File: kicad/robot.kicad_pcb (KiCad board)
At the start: 2 copper layers, 0.4 x 3 mm, 48 parts, among them J2 Adafruit Coil Jumper, J3 Adafruit Coil Jumper, M5 Motor_DC, M6 Motor_DC, M7 Motor_DC, M8 Motor_DC, Q2 NMOS, U10 GY-521, U12 NCP176AMX330TCG, U13 DRV8833PW, U6 DRV8833PW, U8 ESP32-DEVKITC, U9 MCP73831-2-OT

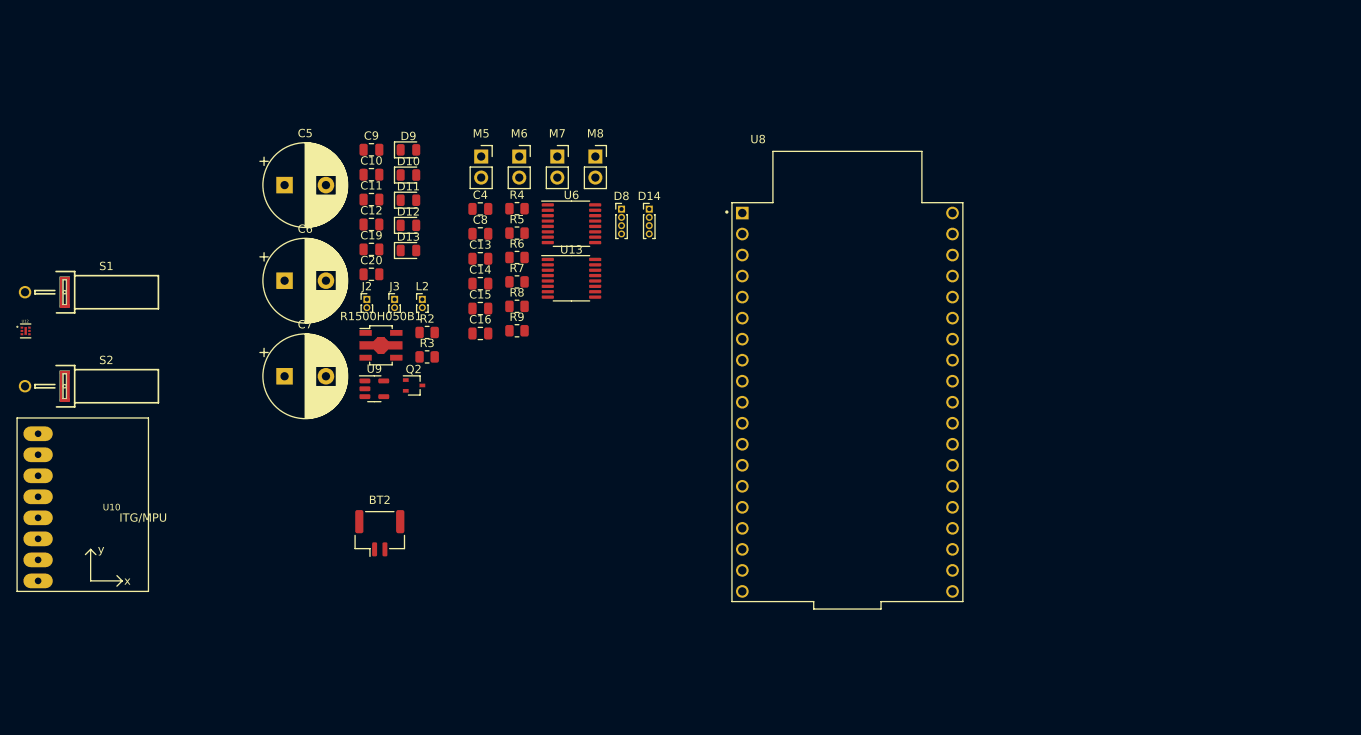
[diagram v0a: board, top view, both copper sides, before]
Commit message: Add board layout
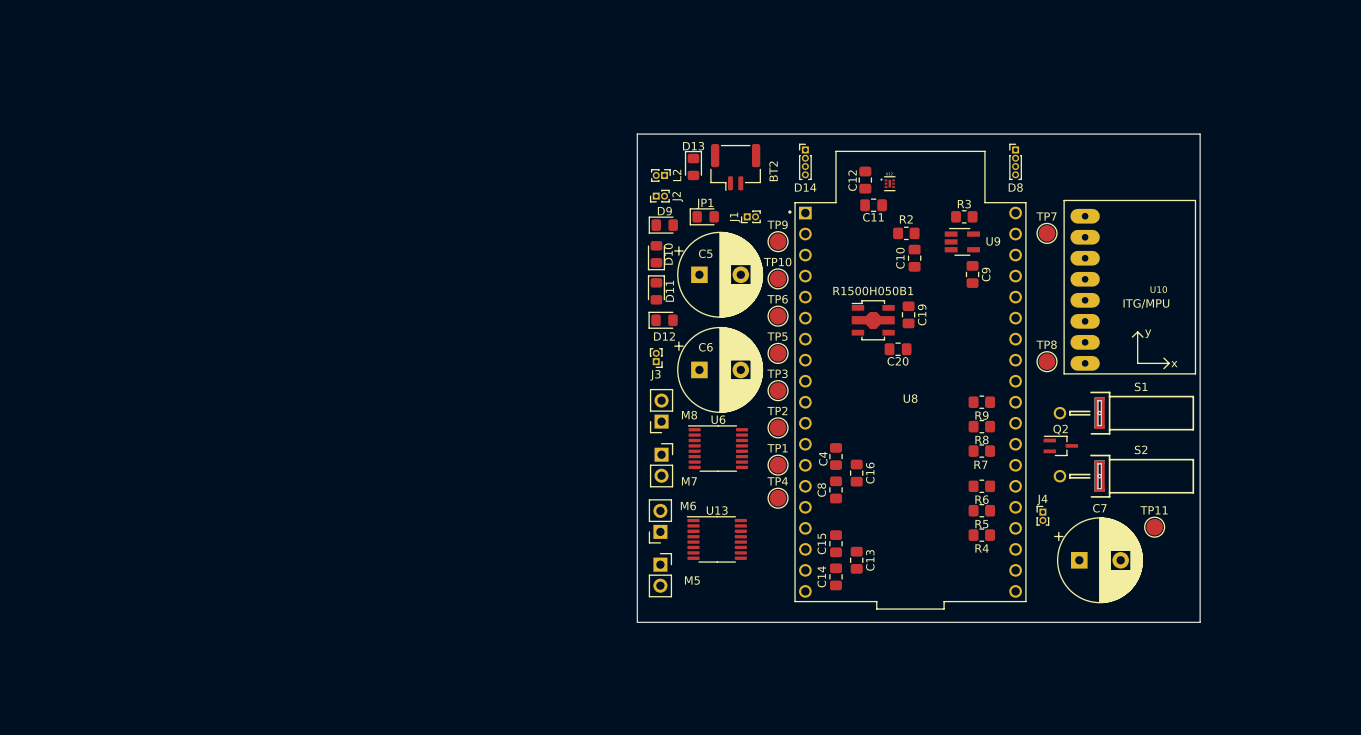
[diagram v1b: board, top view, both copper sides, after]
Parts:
- added J1: Adafruit Coil Jumper, Connector_PinHeader_1.00mm:PinHeader_1x02_P1.00mm_Vertical, F.Cu at (170.8, 66.5)
- added J4: Adafruit Coil Jumper, Connector_PinHeader_1.00mm:PinHeader_1x02_P1.00mm_Vertical, F.Cu at (206.5, 102.2)
- added JP1: SolderJumper_2_Open, Diode_SMD:D_0805_2012Metric_Pad1.15x1.40mm_HandSolder, F.Cu at (165.8, 66.5)
- added TP1: TestPoint, TestPoint:TestPoint_Pad_D2.0mm, F.Cu at (174.5, 96.5)
- added TP10: TestPoint, TestPoint:TestPoint_Pad_D2.0mm, F.Cu at (174.5, 74.0)
- added TP11: TestPoint, TestPoint:TestPoint_Pad_D2.0mm, F.Cu at (220.0, 104.0)
- added TP2: TestPoint, TestPoint:TestPoint_Pad_D2.0mm, F.Cu at (174.5, 92.0)
- added TP3: TestPoint, TestPoint:TestPoint_Pad_D2.0mm, F.Cu at (174.5, 87.5)
- added TP4: TestPoint, TestPoint:TestPoint_Pad_D2.0mm, F.Cu at (174.5, 100.5)
- added TP5: TestPoint, TestPoint:TestPoint_Pad_D2.0mm, F.Cu at (174.5, 83.0)
- added TP6: TestPoint, TestPoint:TestPoint_Pad_D2.0mm, F.Cu at (174.5, 78.5)
- added TP7: TestPoint, TestPoint:TestPoint_Pad_D2.0mm, F.Cu at (207.0, 68.5)
- added TP8: TestPoint, TestPoint:TestPoint_Pad_D2.0mm, F.Cu at (207.0, 84.0)
- added TP9: TestPoint, TestPoint:TestPoint_Pad_D2.0mm, F.Cu at (174.5, 69.5)
- C10, C11, C12, C13, C14, C15, C16, C19, C20, C4, C8, C9: footprint Capacitor_SMD:C_0805_2012Metric -> Capacitor_SMD:C_0805_2012Metric_Pad1.18x1.45mm_HandSolder
- D10, D11, D12, D9: footprint Diode_SMD:D_0805_2012Metric -> Diode_SMD:D_0805_2012Metric_Pad1.15x1.40mm_HandSolder
- D13: footprint LED_SMD:LED_0805_2012Metric -> LED_SMD:LED_0805_2012Metric_Pad1.15x1.40mm_HandSolder
- Q2: footprint Package_TO_SOT_SMD:SOT-323_SC-70 -> Package_TO_SOT_SMD:SOT-323_SC-70_Handsoldering
- R2, R3, R4, R5, R6, R7, R8, R9: footprint Resistor_SMD:R_0805_2012Metric -> Resistor_SMD:R_0805_2012Metric_Pad1.20x1.40mm_HandSolder
- U9: footprint Package_TO_SOT_SMD:SOT-23-5 -> Package_TO_SOT_SMD:SOT-23-5_HandSoldering
- moved U10 129.2 mm to (220.5, 75.3)
- moved S1 125.9 mm to (213.4, 90.2)
- moved S2 125.5 mm to (213.4, 97.8)
- moved U12 105.9 mm to (188.0, 62.5)
- moved C7 98.6 mm to (210.9, 108.0)
- moved Q2 78.5 mm to (208.7, 94.2)
- moved C9 74.2 mm to (198.0, 73.5), turned to -90 degrees
- moved U9 73.2 mm to (196.8, 69.5)
- moved R4 68.6 mm to (199.1, 105.0), turned to 180 degrees
- moved R3 67.1 mm to (197.0, 66.5), turned to 180 degrees
- moved C10 66.4 mm to (191.0, 71.5), turned to 90 degrees
- moved R5 65.4 mm to (199.1, 102.0), turned to 180 degrees
- moved C19 65.4 mm to (190.3, 78.3), turned to -90 degrees
- moved C20 64.3 mm to (189.0, 82.5)
- moved R6 62.6 mm to (199.1, 99.1), turned to 180 degrees
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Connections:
- BT2 pad 2: /Temporary/GND -> Net-(BT2--)
- C10 pad 2: /Temporary/GND -> Net-(BT2--)
- C19 pad 1: /Temporary/5V -> Net-(D13-A)
- C19 pad 2: /Temporary/GND -> Net-(D12-A)
- C20 pad 1: /Temporary/5V -> Net-(D10-K)
- C20 pad 2: /Temporary/GND -> Net-(D12-A)
- C6 pad 2: /Temporary/GND -> Net-(D12-A)
- C7 pad 1: /Temporary/5V -> Net-(D10-K)
- C9 pad 1: /Temporary/5V -> Net-(D13-A)
- C9 pad 2: /Temporary/GND -> Net-(D12-A)
- D10 pad 1: /Temporary/5V -> Net-(D10-K)
- D11 pad 1: /Temporary/5V -> Net-(D10-K)
- D12 pad 2: /Temporary/GND -> Net-(D12-A)
- D13 pad 2: /Temporary/5V -> Net-(D13-A)
- D9 pad 2: /Temporary/GND -> Net-(D12-A)
- J2 pad 1: /Temporary/5V -> Net-(D10-K)
- J2 pad 2: /Temporary/GND -> Net-(D12-A)
- J3 pad 1: /Temporary/5V -> Net-(D13-A)
- J3 pad 2: /Temporary/GND -> Net-(D12-A)
- Q2 pad 1: /Temporary/GND -> Net-(BT2--)
- R1500H050B1 pad 1: /Temporary/5V -> Net-(D10-K)
- R1500H050B1 pad 2: /Temporary/GND -> Net-(D12-A)
- R1500H050B1 pad 3: /Temporary/GND -> Net-(D12-A)
- R1500H050B1 pad 4: /Temporary/5V -> Net-(D10-K)
- R1500H050B1 pad 5: /Temporary/5V -> Net-(D13-A)
- R3 pad 2: /Temporary/GND -> Net-(BT2--)
- S1 pad 2: /Temporary/GND -> Net-(BT2--)
- U12 pad 7: unconnected-(U12-EXP-Pad7) -> /Temporary/Controller/GND
- U9 pad 2: /Temporary/GND -> Net-(BT2--)
- U9 pad 4: /Temporary/5V -> Net-(D13-A)
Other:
- board size 0.4 x 3 mm -> 68 x 59 mm

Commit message: Start adding PCB traces
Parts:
- moved C7 64.3 mm to (165.5, 62.5)
- moved D13 46.7 mm to (211.0, 62.0)
- moved BT2 46.6 mm to (216.0, 60.5)
- moved TP4 12.0 mm to (174.5, 88.5)
- moved JP1 9.16 mm to (160.5, 59.0)
- moved TP1 5.50 mm to (174.5, 102.0)
- moved TP2 5.50 mm to (174.5, 97.5)
- moved TP3 5.50 mm to (174.5, 93.0)
- moved J1 4.22 mm to (174.5, 64.5), turned to 0 degrees
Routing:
- net Net-(BT2--): track 0.00 -> 115.9 mm
- net Net-(D13-A): track 0.00 -> 95.4 mm
- net Net-(D12-A): track 0.00 -> 89.6 mm
- net /Temporary/Controller/VBAT: track 0.00 -> 79.3 mm
- net /Temporary/Controller/GND: track 0.00 -> 73.1 mm
- net Net-(D10-K): track 0.00 -> 60.5 mm
- net Net-(D11-A): track 0.00 -> 52.3 mm
- net /Temporary/Controller/3V3: track 0.00 -> 40.1 mm
- net Net-(D13-K): track 0.00 -> 40.1 mm
- net /Temporary/Controller/MOSTRIG: track 0.00 -> 35.5 mm
- net Net-(U6-VCP): track 0.00 -> 19.4 mm
- net Net-(D10-A): track 0.00 -> 15.8 mm
- net Net-(U8-IO5): track 0.00 -> 15.3 mm
- net Net-(U13-VCP): track 0.00 -> 13.4 mm
- net Net-(U6-VINT): track 0.00 -> 13.0 mm
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
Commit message: So many DRC errors
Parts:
- added F1: Fuse, Fuse:Fuse_0805_2012Metric_Pad1.15x1.40mm_HandSolder, F.Cu at (174.8, 58.8)
- added F2: Fuse, Fuse:Fuse_0805_2012Metric_Pad1.15x1.40mm_HandSolder, F.Cu at (206.2, 58.8)
- D14, D8: footprint Connector_PinHeader_1.00mm:PinHeader_1x04_P1.00mm_Vertical -> Connector_PinSocket_2.54mm:PinSocket_1x04_P2.54mm_Vertical
- J1, J2, J3, J4, L2: footprint Connector_PinHeader_1.00mm:PinHeader_1x02_P1.00mm_Vertical -> Connector_PinSocket_2.54mm:PinSocket_1x02_P2.54mm_Vertical
- moved D14 62.9 mm to (213.0, 110.6), turned to 90 degrees
- moved D8 48.9 mm to (212.9, 106.4), turned to 90 degrees
- moved J1 28.3 mm to (202.4, 59.7)
- moved J2 19.1 mm to (178.8, 62.0), turned to 180 degrees
- moved TP11 18.5 mm to (206.8, 91.0)
- moved JP1 15.0 mm to (174.8, 63.6), turned to -90 degrees
- moved Q2 8.44 mm to (215.0, 88.6)
- moved J4 5.98 mm to (207.6, 108.1)
- moved TP7 5.73 mm to (206.4, 62.8)
- moved S1 5.07 mm to (210.8, 94.6)
- moved U10 3.80 mm to (216.7, 75.5)
- moved S2 3.78 mm to (210.8, 100.6)
- moved TP8 3.61 mm to (206.8, 87.6)
- moved L2 1.11 mm to (160.6, 60.4), turned to 0 degrees
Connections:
- BT2 pad 1: /Temporary/Controller/VBAT -> Net-(BT2-+)
- C10 pad 1: /Temporary/Controller/VBAT -> Net-(BT2-+)
- C20 pad 1: Net-(D10-K) -> Net-(J2-Pin_1)
- J1 pad 1: /Temporary/Controller/VBAT -> Net-(BT2-+)
- J2 pad 1: Net-(D10-K) -> Net-(J2-Pin_1)
- R1500H050B1 pad 1: Net-(D10-K) -> Net-(J2-Pin_1)
- R1500H050B1 pad 4: Net-(D10-K) -> Net-(J2-Pin_1)
- U9 pad 3: /Temporary/Controller/VBAT -> Net-(BT2-+)
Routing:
- net Net-(BT2--): track 115.9 -> 0.00 mm
- net Net-(D13-A): track 95.4 -> 0.00 mm
- net Net-(D12-A): track 89.6 -> 0.00 mm
- net /Temporary/Controller/VBAT: track 79.3 -> 0.00 mm
- net /Temporary/Controller/GND: track 73.1 -> 0.00 mm
- net Net-(D10-K): track 60.5 -> 0.00 mm
- net Net-(D11-A): track 52.3 -> 0.00 mm
- net /Temporary/Controller/3V3: track 40.1 -> 0.00 mm
- net Net-(D13-K): track 40.1 -> 0.00 mm
- net /Temporary/Controller/MOSTRIG: track 35.5 -> 0.00 mm
- net Net-(U6-VCP): track 19.4 -> 0.00 mm
- net Net-(D10-A): track 15.8 -> 0.00 mm
- net Net-(U8-IO5): track 15.3 -> 0.00 mm
- net Net-(U13-VCP): track 13.4 -> 0.00 mm
- net Net-(U6-VINT): track 13.0 -> 0.00 mm
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- added copper zone on B.Cu, net /Temporary/Controller/GND
- added copper zone on F.Cu, net /Temporary/Controller/VBAT
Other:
- board size 68 x 59 mm -> 71.7 x 62.3 mm

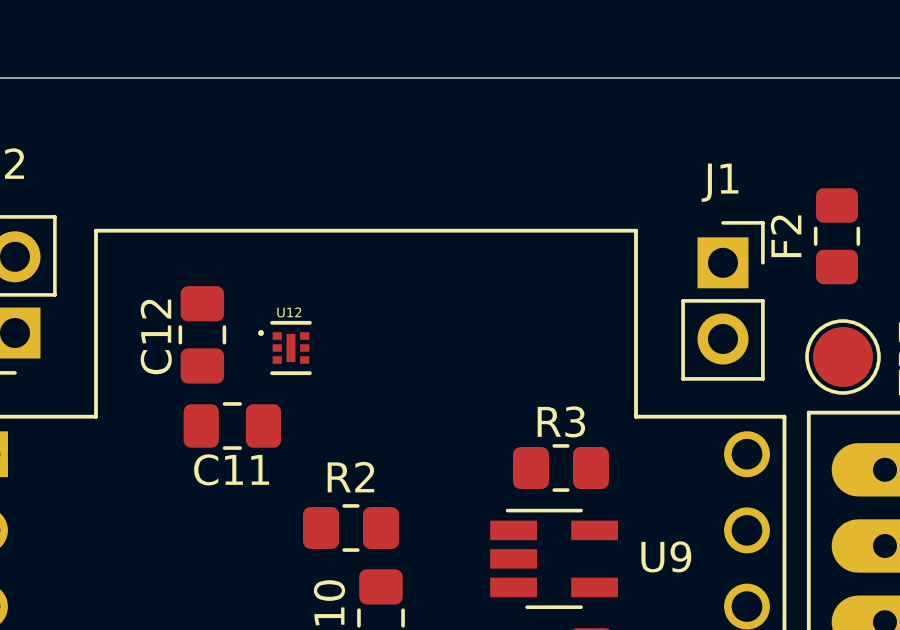
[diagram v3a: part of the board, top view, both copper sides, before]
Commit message: Add new 3.3V regulator
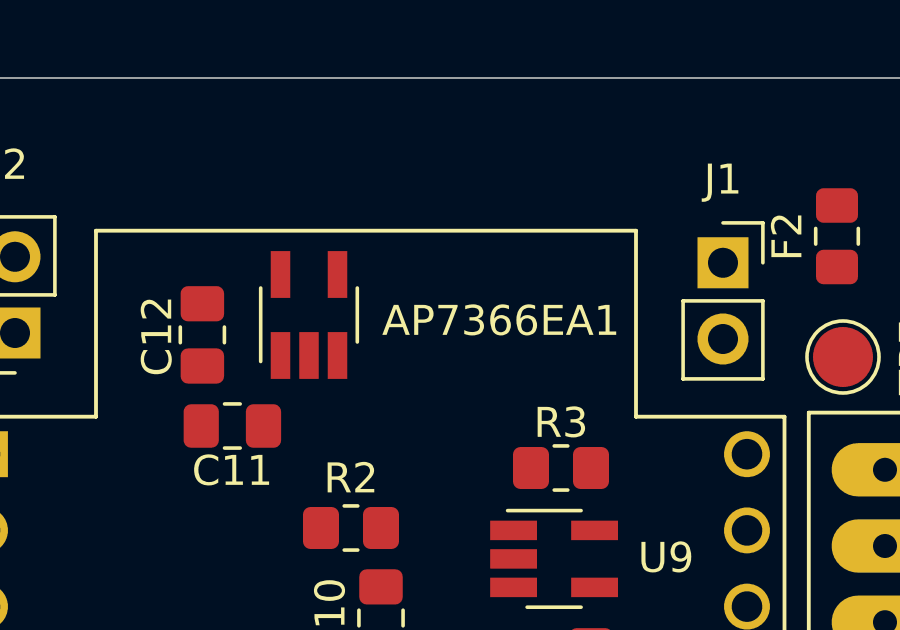
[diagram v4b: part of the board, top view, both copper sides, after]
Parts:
- removed U12: NCP176AMX330TCG, NCP176AMX330TCG:PSON40P120X120X45-7N_NCP176AMX330TCG
- added AP7366EA1: ~, Package_TO_SOT_SMD:SOT-23-5_HandSoldering, F.Cu at (188.6, 61.4)

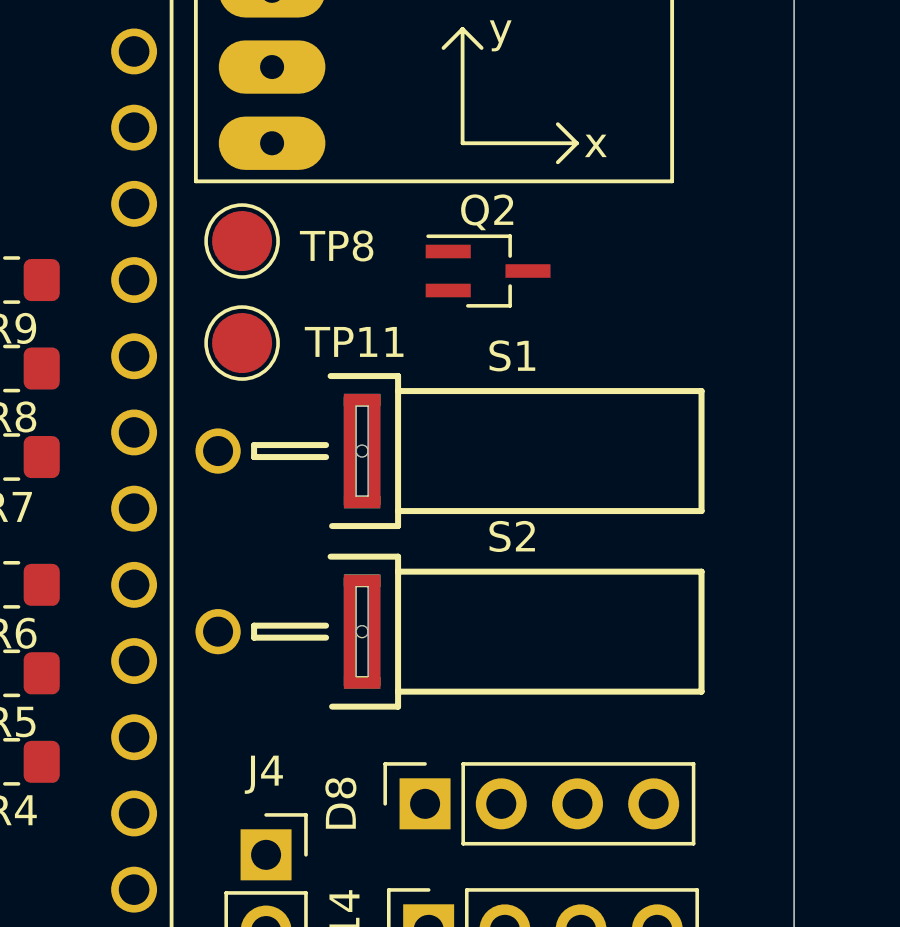
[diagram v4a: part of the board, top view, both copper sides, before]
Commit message: Add tilt switch
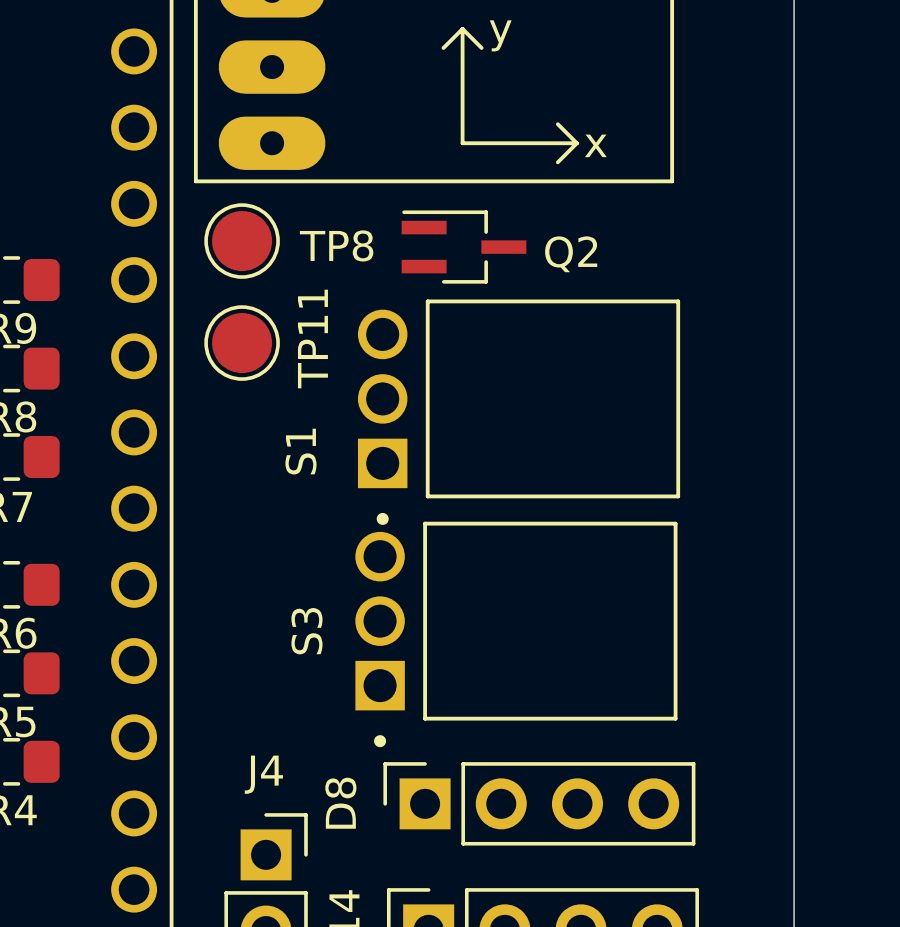
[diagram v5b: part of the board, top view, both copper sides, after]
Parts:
- removed S2: RB-231X2, RB-231X2:SW_RB-231X2
- added S3: TM1000Q, TM1000Q:SW_TM1000Q, F.Cu at (211.4, 100.3)
- S1: value RB-231X2 -> TM1000Q; footprint RB-231X2:SW_RB-231X2 -> TM1000Q:SW_TM1000Q
- moved S1 1.87 mm to (211.5, 92.9), turned to 90 degrees
- moved Q2 1.13 mm to (214.2, 87.8)
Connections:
- Q2 pad 3: /Temporary/Controller/GND -> Net-(Q2-S)
- S1 pad 1: /Temporary/Controller/GND -> /Temporary/Controller/3V3
- S1 pad 2: Net-(BT2--) -> Net-(U8-IO5)

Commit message: First PCB Layout complete
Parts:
- removed S3: TM1000Q, TM1000Q:SW_TM1000Q
- added D1: D, Diode_SMD:D_0805_2012Metric_Pad1.15x1.40mm_HandSolder, F.Cu at (210.6, 87.0)
- added R1: 2k, Resistor_SMD:R_0805_2012Metric_Pad1.20x1.40mm_HandSolder, F.Cu at (206.8, 94.6)
- added S2: TM1000Q, TM1000Q:SW_TM1000Q, F.Cu at (211.5, 100.3)
- added TP12: TestPoint, TestPoint:TestPoint_Pad_D2.0mm, F.Cu at (207.4, 102.4)
- moved Q2 1.88 mm to (216.1, 87.6)
- moved AP7366EA1 1.05 mm to (188.7, 60.4), turned to 180 degrees
- moved J3 0.86 mm to (160.4, 84.6)
- moved R4 0.84 mm to (199.1, 105.8)
- moved R9 0.50 mm to (199.1, 88.4)
- moved R7 0.40 mm to (199.1, 95.2)
- moved R5 0.39 mm to (199.1, 102.4)
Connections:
- Q2 pad 1: Net-(BT2--) -> /Temporary/Controller/GND
- Q2 pad 2: /Temporary/Controller/MOSTRIG -> Net-(D1-K)
- Q2 pad 3: Net-(Q2-S) -> Net-(BT2--)
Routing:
- net Net-(BT2--): track 0.00 -> 127.6 mm, vias 0 -> 5
- net /Temporary/Controller/3V3: track 0.00 -> 114.9 mm, vias 0 -> 4
- net Net-(D12-A): track 0.00 -> 112.8 mm
- net Net-(D13-A): track 0.00 -> 80.0 mm, vias 0 -> 2
- net Net-(U13-BIN1): track 0.00 -> 73.1 mm, vias 0 -> 4
- net Net-(D11-A): track 0.00 -> 51.7 mm
- net Net-(U13-BIN2): track 0.00 -> 49.2 mm, vias 0 -> 2
- net Net-(D14-RK): track 0.00 -> 46.4 mm
- net Net-(D8-RK): track 0.00 -> 45.1 mm, vias 0 -> 2
- net /Temporary/Controller/GND: track 0.00 -> 44.4 mm, vias 0 -> 11
- net Net-(BT2-+): track 0.00 -> 43.2 mm
- net Net-(U13-nFAULT): track 0.00 -> 41.1 mm, vias 0 -> 1
- net Net-(U6-nFAULT): track 0.00 -> 40.7 mm, vias 0 -> 2
- net Net-(J2-Pin_1): track 0.00 -> 40.2 mm, vias 0 -> 2
- net Net-(U6-VCP): track 0.00 -> 38.3 mm
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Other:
- board size 71.7 x 62.3 mm -> 67.6 x 59.8 mm
